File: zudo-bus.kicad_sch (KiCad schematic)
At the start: 0 parts

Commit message: Add global labels and wires for power distribution schematic
- Add global labels for all 8 IDC headers (U2, U5-U11):
  - -12V rail, GND rail, +12V rail on left/right sides
  - +5V rail, CV rail, GATE rail on left/right sides
- Add labels for FASTON connectors (U12-U15): GND, +12V, -12V, +5V
- Add labels for screw terminals (P1, P2): GND
- Add input labels at fuse inputs connecting to input connectors
- Add wires from input labels to connector pins

Circuit flow: Input connectors → Fuses → Rail distribution → IDC headers

Co-Authored-By: Claude Opus 4.5 <noreply@anthropic.com>
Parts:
- added C1, C10, C11, C12, C13, C14, C15, C16, C2, C20, C23, C3, C4, C5, C6, C7, C8, C9: CC0603KRX7R9BB104, easyeda2kicad:C0603, symbol zudo-bus:CC0603KRX7R9BB104
- added C17, C18, C19, C22: CL21A226MAQNNNE, zudo-bus:C0805, symbol zudo-bus-new-protection:CL21A226MAQNNNE
- added C21: CL21A106KAYNNNE, samsung-caps:C0805, symbol samsung-caps:CL21A106KAYNNNE
- added D1, D3: SMF12CA_C353317, zudo-bus:SOD-123FL_L2.8-W1.8-LS3.7-BI, symbol zudo-bus-new-protection:SMF12CA_C353317
- added D2: SMF5.0CA_C908214, :SOD-123_L2.8-W1.8-LS3.7-BI, symbol zudo-bus-protection:SMF5.0CA_C908214
- added D4, D5: SS14, zudo-bus:SMA_L4.2-W2.6-LS5.0-RD_1, symbol zudo-bus-new-protection:SS14
- added D6, D7, D8, D9: SM4007PL, easyeda2kicad:SOD-123F_L2.8-W1.8-LS3.7-RD, symbol zudo-bus:SM4007PL
- added F1, F2: BSMD1812-200-30V, :F1812, symbol zudo-bus-protection:BSMD1812-200-30V
- added F3, F4: BSMD1812-150-33V, :F1812, symbol zudo-bus-protection:BSMD1812-150-33V
- added H1: Header-Male-2.54_1x3, easyeda2kicad:HDR-TH_3P-P2.54-V-M-1, symbol zudo-bus:Header-Male-2.54_1x3
- added LED1: KT-0603R, easyeda2kicad:LED0603-RD, symbol zudo-bus:KT-0603R
- added P1, P2: WJ500V-5.08-2P-14-00A, easyeda2kicad:CONN-TH_2P-P5.00_WJ500V-5.08-2P, symbol zudo-bus:WJ500V-5.08-2P-14-00A
- added R1: 0805W8J0102T5E, easyeda2kicad:R0805, symbol zudo-bus:0805W8J0102T5E
- added TP1: TestPoint, symbol Connector:TestPoint
- added U10, U11, U2, U5, U6, U7, U8, U9: 2541WR-2X08P, easyeda2kicad:HDR-TH_16P-P2.54-H-M-R2-C8-S2.54, symbol zudo-bus:2541WR-2X08P
- added U12, U13, U14, U15: 1217754-1, easyeda2kicad:CONN-TH_1217754-1, symbol zudo-bus:1217754-1
- added U3: YLED0603YG, easyeda2kicad:LED0603-FD, symbol zudo-bus:YLED0603YG
- added U4: NCD1608A1, easyeda2kicad:LED0603-RD, symbol zudo-bus:NCD1608A1
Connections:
- new net +12V in: F1.1, U12.2
- new net +12V rail: F1.2, U10.10, U10.9, U11.10, U11.9, U2.10, U2.9, U5.10, U5.9, U6.10, U6.9, U7.10, U7.9, U8.10, U8.9, U9.10, U9.9
- new net +5V in: F3.1, U14.2
- new net +5V rail: U10.11, U10.12, U11.11, U11.12, U2.11, U2.12, U5.11, U5.12, U6.11, U6.12, U7.11, U7.12, U8.11, U8.12, U9.11, U9.12
- new net -12V in: F2.1, U13.2
- new net -12V rail: F2.2, U10.1, U10.2, U11.1, U11.2, U2.1, U2.2, U5.1, U5.2, U6.1, U6.2, U7.1, U7.2, U8.1, U8.2, U9.1, U9.2
- new net CV rail: U10.13, U10.14, U11.13, U11.14, U2.13, U2.14, U5.13, U5.14, U6.13, U6.14, U7.13, U7.14, U8.13, U8.14, U9.13, U9.14
- new net GATE rail: U10.15, U10.16, U11.15, U11.16, U2.15, U2.16, U5.15, U5.16, U6.15, U6.16, U7.15, U7.16, U8.15, U8.16, U9.15, U9.16
- new net GND in: F4.1, U15.2
- new net GND rail: U10.5, U10.6, U11.5, U11.6, U2.5, U2.6, U5.5, U5.6, U6.5, U6.6, U7.5, U7.6, U8.5, U8.6, U9.5, U9.6

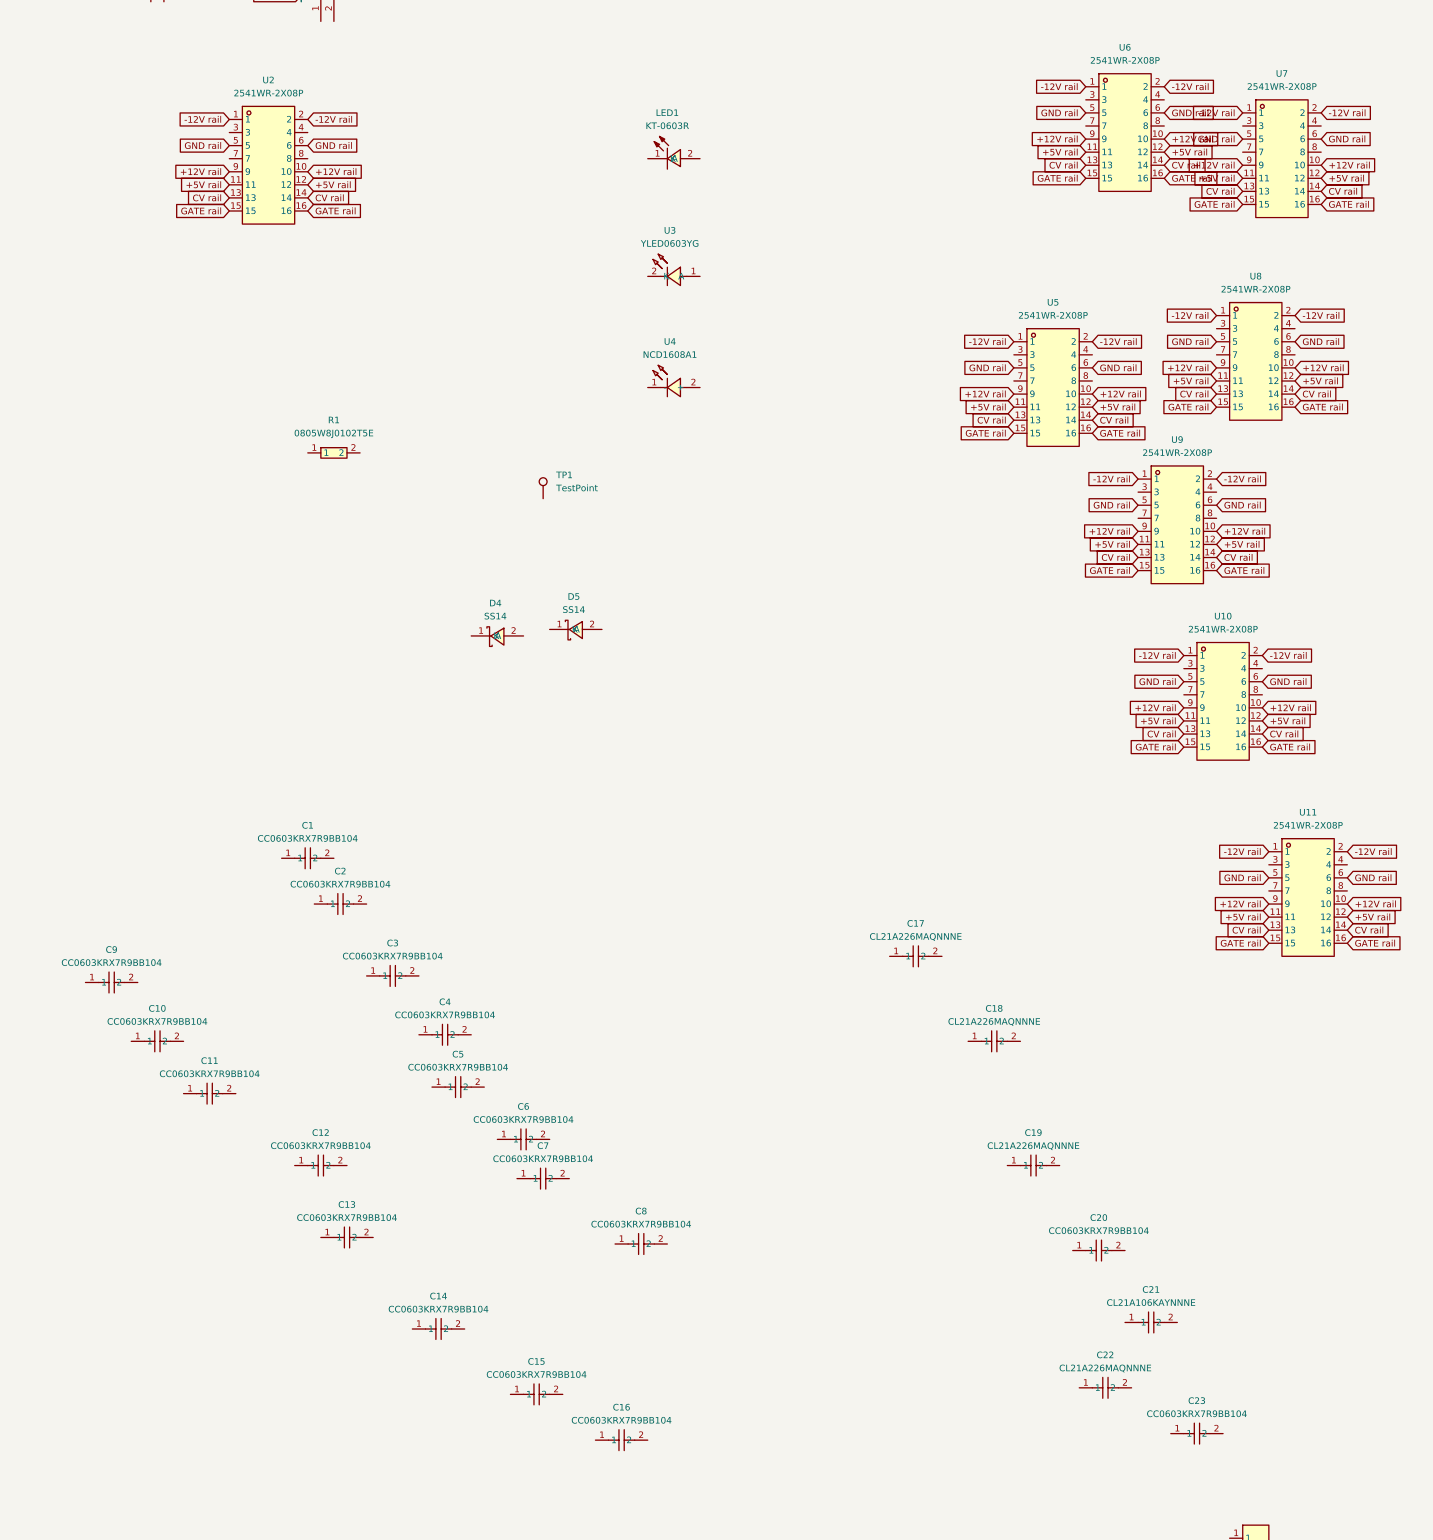
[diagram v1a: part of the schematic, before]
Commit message: Add global labels for capacitor power connections
Added 46 global labels to connect all bypass capacitors (C1-C23):
- Pin 2 of all capacitors connected to GND rail
- Pin 1 connected to respective power rails:
  - C1-C4: LDO related (+12V, +5V)
  - C5: +12V bulk capacitor
  - C6: -12V bulk capacitor
  - C7-C14: +12V per-header decoupling
  - C15-C22: -12V per-header decoupling
  - C23: +5V bulk capacitor

This reduces ERC errors from 91 to 45.

Co-Authored-By: Claude Opus 4.5 <noreply@anthropic.com>
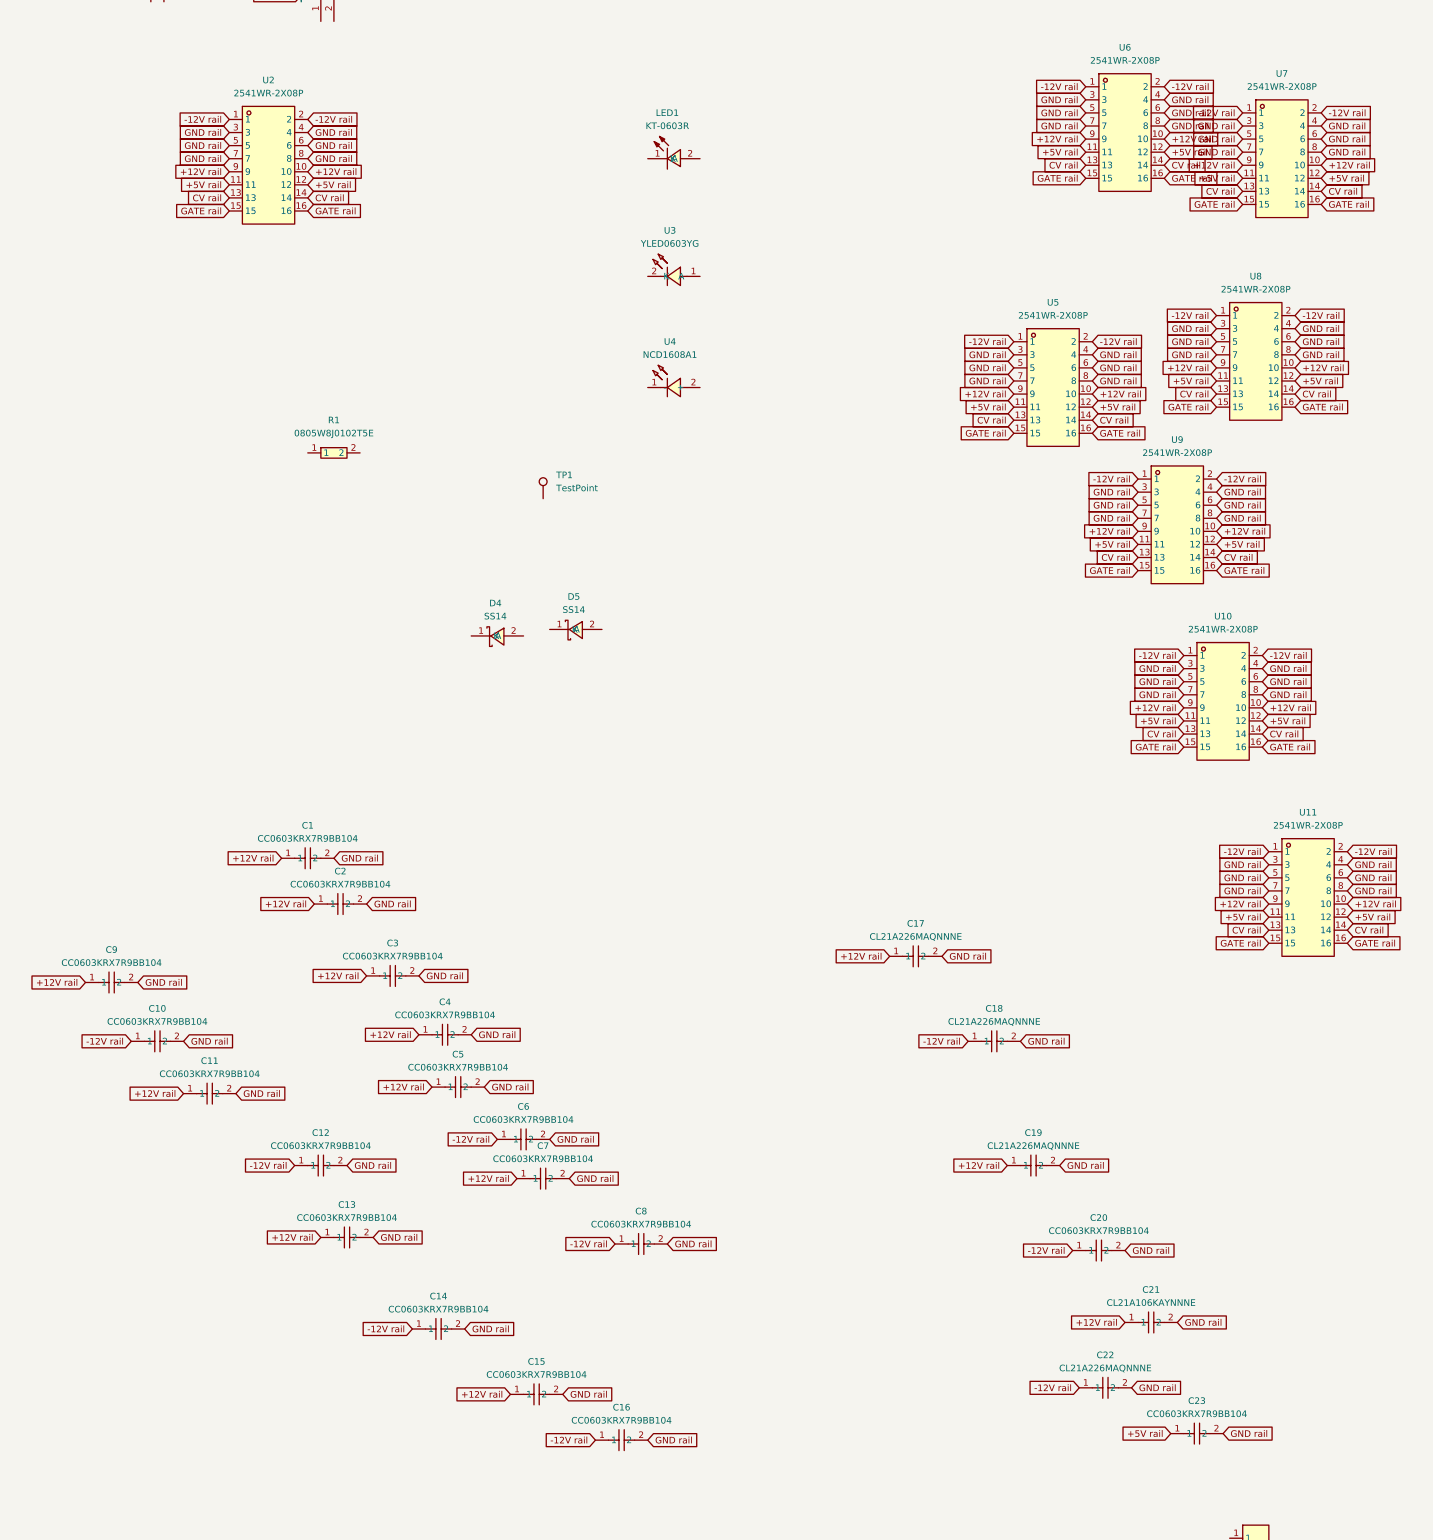
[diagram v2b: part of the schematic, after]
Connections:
- net +12V rail: now also C1.1, C11.1, C13.1, C15.1, C17.1, C19.1, C2.1, C21.1, C3.1, C4.1, C5.1, C7.1, C9.1
- net +5V rail: now also C23.1
- net -12V rail: now also C10.1, C12.1, C14.1, C16.1, C18.1, C20.1, C22.1, C6.1, C8.1
- net GND rail: now also C1.2, C10.2, C11.2, C12.2, C13.2, C14.2, C15.2, C16.2, C17.2, C18.2, C19.2, C2.2, C20.2, C21.2, C22.2, C23.2, C3.2, C4.2, C5.2, C6.2, C7.2, C8.2, C9.2, U10.3, U10.4, U10.7, U10.8, U11.3, U11.4, U11.7, U11.8, U2.3, U2.4, U2.7, U2.8, U5.3, U5.4, U5.7, U5.8, U6.3, U6.4, U6.7, U6.8, U7.3, U7.4, U7.7, U7.8, U8.3, U8.4, U8.7, U8.8, U9.3, U9.4, U9.7, U9.8

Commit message: Add global labels to connect protection circuits and terminals
Connect remaining unconnected components to their respective power rails:
- TVS diodes D1, D2, D3 (+12V, GND, -12V protection)
- Reverse protection diodes D6-D9 (all rails)
- Schottky OR-ing diodes D4, D5
- Screw terminals P1, P2 (power input)
- FASTON terminals U12-U15 (power output)
- LEDs and indicator circuits (LED1, U3, U4, R1)
- Jumper H1 (+5V source selection)
- Fuses F3, F4 (rail protection)
- Test point TP1 (GND)

Reduces ERC errors from 45 to 5 (remaining are pin_not_driven
symbol type issues, not connection issues).

Co-Authored-By: Claude Opus 4.5 <noreply@anthropic.com>
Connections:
- net +12V in: now also D6.1 (C), P1.1, U12.1
- net +12V rail: now also D1.1 (A2), TP1.1, U3.1 (A)
- net +5V in: now also D5.2 (A), D8.1 (C), H1.3, U14.1
- net +5V rail: now also D2.1, F3.2, H1.2, U4.2 (+)
- net -12V in: now also D7.2 (A), P2.1, U13.1
- net -12V rail: now also D3.1 (A2), R1.2
- net GND in: now also P1.2, P2.2, U15.1
- net GND rail: now also D1.2 (A1), D2.2, D3.2 (A1), D4.2 (A), D6.2 (A), D7.1 (C), D8.2 (A), D9.2 (A), F4.2, LED1.2 (A), U3.2 (K), U4.1 (-)
- net LDO out: now reaches D9.1 (C)
- net LDO out: now also D4.1 (K), H1.1
- net +5V JP1: now reaches D5.1 (K)
- net LED1_R1: now reaches LED1.1 (K)
- net LED1_R1: now also R1.1

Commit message: Add wires between component pins and labels
Following schematic best practice, add short wires (5.08mm) connecting
component pins to their global labels instead of placing labels directly
on pins. This makes the schematic:
- More readable with explicit visual connections
- Easier to reorganize (components can move, labels stay)
- Following standard schematic conventions

Added 228 wires for all global labels. Labels moved to wire endpoints.

Known issue: Some labels overlap on components with vertical pin
arrangements (FASTON terminals, screw terminals, jumper H1, etc.)
- Will be fixed in follow-up commit

Co-Authored-By: Claude Opus 4.5 <noreply@anthropic.com>
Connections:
- net +5V in is gone; now on net +12V in: D5.2 (A), D8.1 (C), F3.1, H1.3, U14.1, U14.2
- net -12V in is gone; now on net +12V in: D7.2 (A), F2.1, P2.1, U13.1, U13.2
- net GND in is gone; now on net +12V in: F4.1, P1.2, P2.2, U15.1, U15.2
